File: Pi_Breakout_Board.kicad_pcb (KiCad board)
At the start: 2 copper layers, 56.5 x 65 mm, 70 parts, among them J1 Raspberry_Pi_2_3, J2 Conn_02x04_Odd_Even heater he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, J3 Conn_02x08_Odd_Even thermisto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, J4 Screw_Terminal_01x02, J5 Conn_01x08_Male, J6 Conn_01x08_Male, J7 Conn_01x05_Male uart breakout, Q1 Q_NMOS_GDSD, Q2 Q_NMOS_GDSD, Q3 Q_NMOS_GDSD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

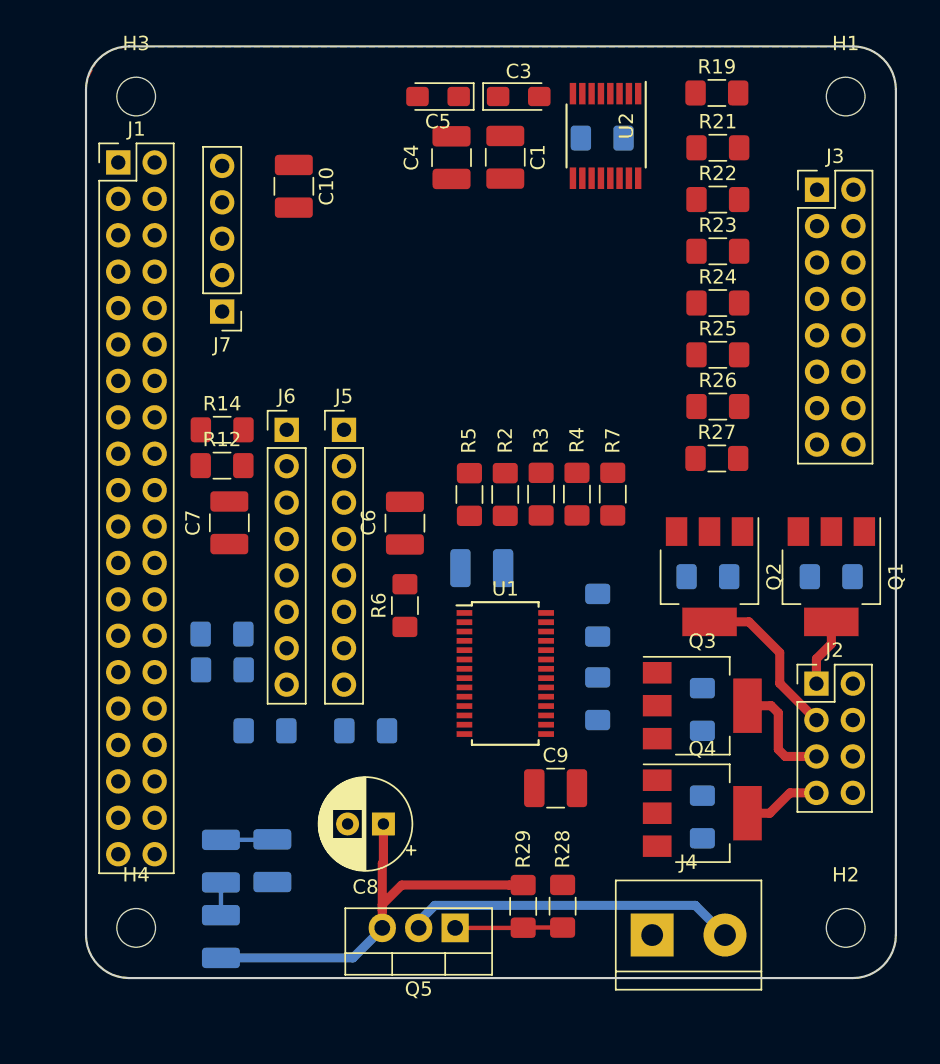
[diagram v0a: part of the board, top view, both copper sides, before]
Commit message: move the PCA9865 from I2C1 to I2C0. Routing saga continues
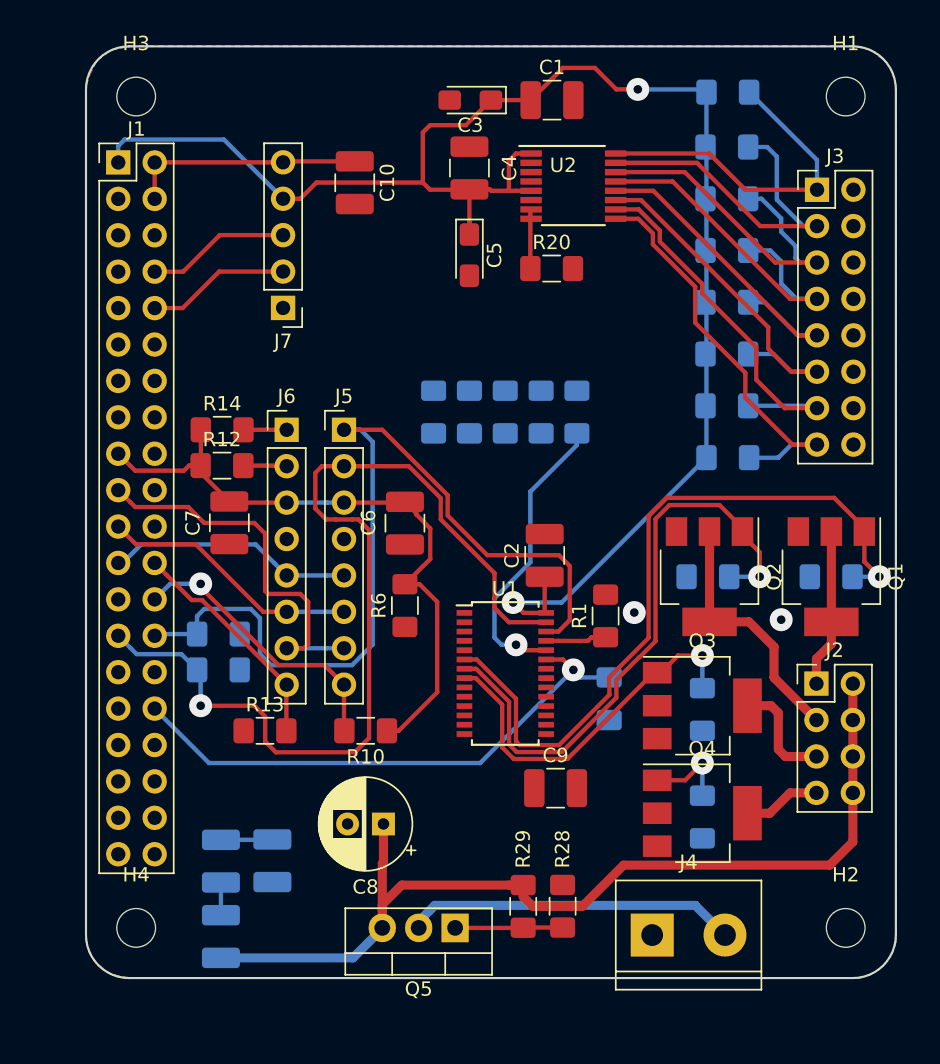
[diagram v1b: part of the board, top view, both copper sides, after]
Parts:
- C2, R1, R10, R13, R20: moved to F.Cu
- R19, R2, R21, R22, R23, R24, R25, R26, R27, R3, R4, R5, R7: moved to B.Cu
- moved C5 11.3 mm to (76.8, 99.6), turned to 270 degrees
- moved R20 9.76 mm to (82.5, 100.5)
- moved R2 7.62 mm to (74.2, 110.5)
- moved R5 7.62 mm to (81.8, 110.5)
- moved R3 7.60 mm to (76.8, 110.5)
- moved R4 7.60 mm to (79.2, 110.5)
- moved R7 6.25 mm to (84.2, 110.5)
- moved C1 5.15 mm to (82.5, 88.8), turned to 0 degrees
- moved C2 4.48 mm to (82.0, 120.5), turned to 90 degrees
- moved C10 4.26 mm to (68.8, 94.5)
- moved J7 4.26 mm to (63.8, 103.2)
- moved U2 4.16 mm to (84.0, 94.8), turned to 0 degrees
- moved C3 3.38 mm to (76.8, 88.8), turned to 180 degrees
- moved C4 1.45 mm to (76.8, 93.5), turned to 90 degrees
- moved R8 0.80 mm to (86.5, 130.5)
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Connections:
- U1 pad 26: SCL1 -> SCL0
- U1 pad 27: SDA1 -> SDA0
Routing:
- net +3V3: track 0.00 -> 159.2 mm, vias 0 -> 2
- net SDA0: track 0.00 -> 68.1 mm, vias 0 -> 1
- net SCL0: track 0.00 -> 63.2 mm
- net Net-(Q1-Pad1): track 0.00 -> 51.5 mm, vias 0 -> 1
- net Net-(Q2-Pad1): track 0.00 -> 43.1 mm, vias 0 -> 1
- net ~OE: track 0.00 -> 38.4 mm, vias 0 -> 1
- net 28V: track 30.3 -> 67.3 mm
- net Net-(J3-Pad15): track 0.00 -> 28.6 mm
- net MOSI0: track 0.00 -> 27.4 mm
- net Net-(J3-Pad13): track 0.00 -> 26.8 mm
- net Net-(Q3-Pad1): track 0.00 -> 25.9 mm, vias 0 -> 1
- net Net-(J3-Pad11): track 0.00 -> 25.2 mm
- net Net-(J3-Pad3): track 0.00 -> 24.7 mm
- net Net-(J3-Pad7): track 0.00 -> 24.6 mm
- net Net-(J3-Pad5): track 0.00 -> 24.4 mm
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- added copper zone on B.Cu, net GND
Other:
- net class Default: via_dia 0.8 -> 1.6; via_drill 0.4 -> 0.6
- net class Power: via_dia 0.8 -> 1.6; via_drill 0.4 -> 0.6

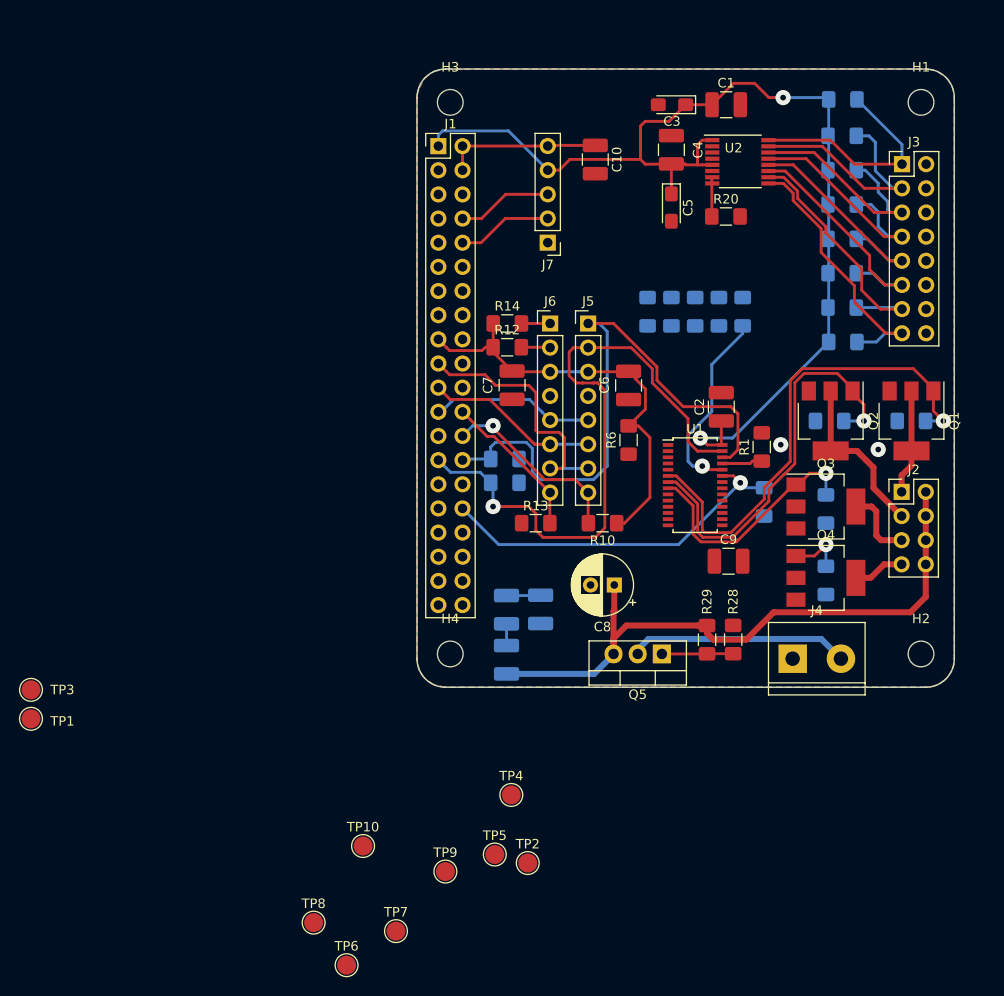
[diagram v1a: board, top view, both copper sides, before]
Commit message: rev3 with corrected header placement in work
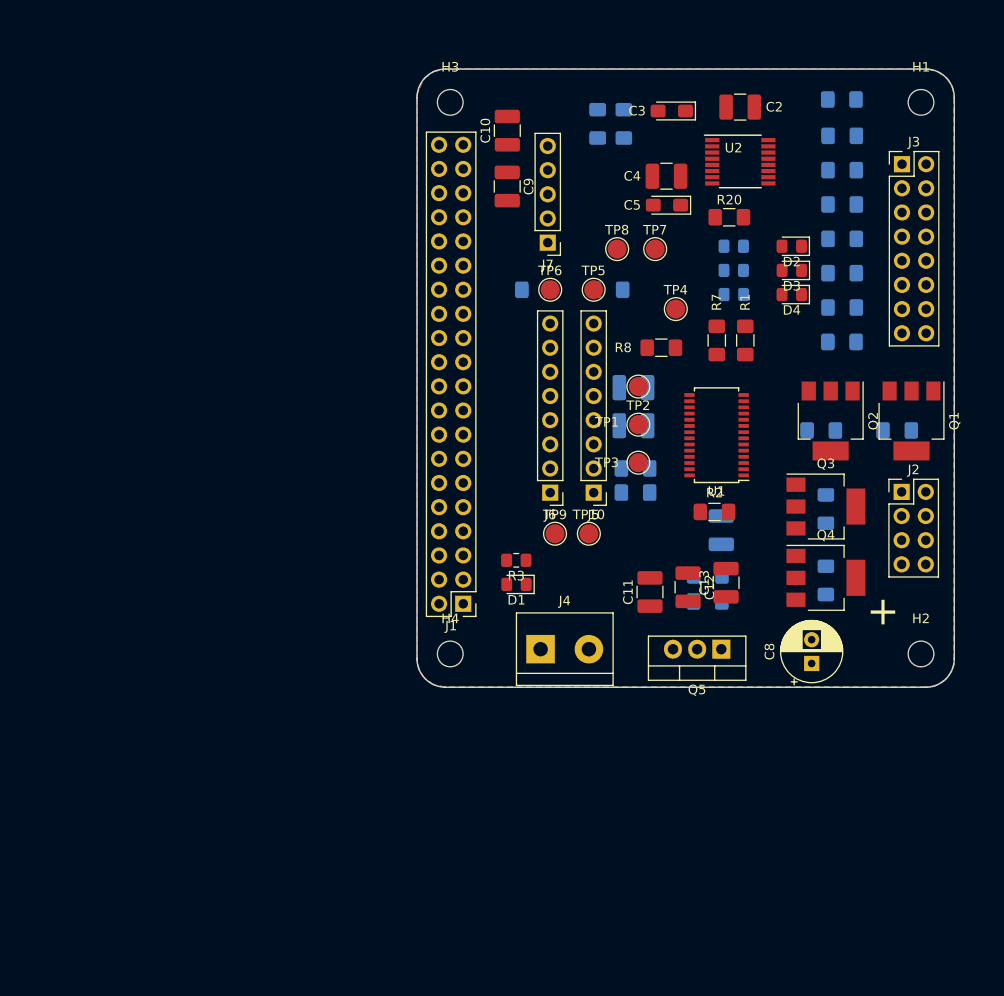
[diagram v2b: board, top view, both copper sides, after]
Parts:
- added D1: LED GREEN, LED_SMD:LED_0805_2012Metric_Pad1.15x1.40mm_HandSolder, F.Cu at (60.5, 139.2)
- added D2: LED GREEN, LED_SMD:LED_0805_2012Metric_Pad1.15x1.40mm_HandSolder, F.Cu at (89.4, 103.6)
- added D3: LED YELLOW, LED_SMD:LED_0805_2012Metric_Pad1.15x1.40mm_HandSolder, F.Cu at (89.4, 106.2)
- added D4: LED RED, LED_SMD:LED_0805_2012Metric_Pad1.15x1.40mm_HandSolder, F.Cu at (89.4, 108.7)
- C1, C6, C7, R10, R12, R13, R14, R28, R29: moved to B.Cu
- C11, C12, C13, R2, R7, R8: moved to F.Cu
- R3: value 10K -> 65R; footprint Resistor_SMD:R_1206_3216Metric_Pad1.42x1.75mm_HandSolder -> Resistor_SMD:R_0805_2012Metric_Pad1.15x1.40mm_HandSolder; moved to F.Cu
- R4, R5: value 10K -> 65R; footprint Resistor_SMD:R_1206_3216Metric_Pad1.42x1.75mm_HandSolder -> Resistor_SMD:R_0805_2012Metric_Pad1.15x1.40mm_HandSolder
- R6: value 10K -> 65R; footprint Resistor_SMD:R_1206_3216Metric_Pad1.42x1.75mm_HandSolder -> Resistor_SMD:R_0805_2012Metric_Pad1.15x1.40mm_HandSolder; moved to B.Cu
- moved TP8 77.7 mm to (71.0, 103.9)
- moved TP7 76.7 mm to (75.0, 103.9)
- moved TP6 74.2 mm to (64.0, 108.2)
- moved TP1 71.0 mm to (73.3, 122.4), turned to 180 degrees
- moved TP3 68.2 mm to (73.3, 126.4), turned to 180 degrees
- moved TP5 60.3 mm to (68.6, 108.2)
- moved TP4 53.9 mm to (77.2, 110.2)
- moved TP2 51.4 mm to (73.3, 118.4), turned to 180 degrees
- moved J1 48.2 mm to (54.9, 141.2), turned to 180 degrees
- moved C9 45.8 mm to (59.5, 97.3), turned to 270 degrees
- moved C1 44.7 mm to (82.0, 133.5), turned to 270 degrees
- moved TP10 40.5 mm to (68.1, 133.9)
- moved TP9 37.3 mm to (64.5, 133.9)
- moved C2 31.6 mm to (84.0, 89.0), turned to 0 degrees
- moved R3 30.8 mm to (60.4, 136.7), turned to 180 degrees
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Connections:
- J1 pad 12: Net-(J1-Pad12) -> LED_GREEN
- J1 pad 16: Net-(J1-Pad16) -> LED_YELLOW
- J1 pad 18: Net-(J1-Pad18) -> LED_RED
- R3 pad 1: Net-(R3-Pad1) -> Net-(D1-Pad1)
- R4 pad 1: Net-(R4-Pad1) -> LED_GREEN
- R4 pad 2: +3V3 -> Net-(D2-Pad2)
- R5 pad 1: Net-(R5-Pad1) -> LED_YELLOW
- R5 pad 2: GND -> Net-(D3-Pad2)
- R6 pad 1: Net-(R6-Pad1) -> LED_RED
- R6 pad 2: +3V3 -> Net-(D4-Pad2)
- U1 pad 2: Net-(R3-Pad1) -> GND
- U1 pad 26: SCL0 -> SCL1
- U1 pad 27: SDA0 -> SDA1
- U1 pad 3: Net-(R4-Pad1) -> +3V3
- U1 pad 4: Net-(R5-Pad1) -> GND
- U1 pad 5: Net-(R6-Pad1) -> +3V3
- U2 pad 2: SDA1 -> SDA0
- U2 pad 3: SCL1 -> SCL0
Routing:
- net +3V3: track 159.2 -> 0.00 mm, vias 2 -> 0
- net SDA0: track 68.1 -> 0.00 mm, vias 1 -> 0
- net 28V: track 67.3 -> 0.00 mm
- net SCL0: track 63.2 -> 0.00 mm
- net Net-(Q1-Pad1): track 51.5 -> 0.00 mm, vias 1 -> 0
- net Net-(Q2-Pad1): track 43.1 -> 0.00 mm, vias 1 -> 0
- net ~OE: track 38.4 -> 0.00 mm, vias 1 -> 0
- net Net-(J3-Pad15): track 28.6 -> 0.00 mm
- net MOSI0: track 27.4 -> 0.00 mm
- net Net-(J3-Pad13): track 26.8 -> 0.00 mm
- net Net-(Q3-Pad1): track 25.9 -> 0.00 mm, vias 1 -> 0
- net Net-(J3-Pad11): track 25.2 -> 0.00 mm
- net Net-(J3-Pad3): track 24.7 -> 0.00 mm
- net Net-(J3-Pad7): track 24.6 -> 0.00 mm
- net Net-(J3-Pad5): track 24.4 -> 0.00 mm
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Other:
- net class Default: trace_width 0.3048 -> 0.4; via_dia 1.6 -> 1.2
- net class Power: trace_width 0.635 -> 1
- rule trace_min: 0.2 -> 0.4
- rule via_min_drill: 0.3 -> 0.6
- rule via_min_size: 0.4 -> 1.2
- board text added: "+"

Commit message: misc routing
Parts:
- removed TP2: TestPoint, TestPoint:TestPoint_Pad_D2.0mm
- added J8: Conn_01x03_Male, Connector_PinHeader_2.54mm:PinHeader_1x03_P2.54mm_Vertical, F.Cu at (63.5, 130.8)
- C10, C9: moved to B.Cu
- J7: value Conn_01x05_Male uart breakout -> Conn_01x02_Female; footprint Connector_PinHeader_2.54mm:PinHeader_1x05_P2.54mm_Vertical -> Connector_PinSocket_2.54mm:PinSocket_1x02_P2.54mm_Horizontal
- R12, R14, R4, R5, R6: moved to F.Cu
- moved R12 50.4 mm to (62.2, 140.2), turned to 180 degrees
- moved C10 49.5 mm to (59.9, 141.0), turned to 0 degrees
- moved R14 45.6 mm to (62.2, 135.9), turned to 180 degrees
- moved J7 42.3 mm to (58.7, 145.3), turned to 90 degrees
- moved R11 39.5 mm to (70.6, 90.1), turned to 270 degrees
- moved C9 38.5 mm to (59.9, 135.9), turned to 0 degrees
- moved TP10 38.2 mm to (59.9, 96.5)
- moved TP9 37.4 mm to (63.5, 96.5)
- moved R9 37.2 mm to (68.1, 90.1), turned to 270 degrees
- moved J6 26.4 mm to (62.7, 103.1), turned to 0 degrees
- moved J5 26.4 mm to (68.1, 103.1), turned to 0 degrees
- moved TP3 20.0 mm to (58.7, 112.8)
- moved C7 18.8 mm to (58.9, 109.7), turned to 270 degrees
- moved TP6 16.3 mm to (62.7, 124.5)
- moved R13 16.3 mm to (61.3, 124.5)
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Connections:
- J1 pad 19: MOSI0 -> Net-(J1-Pad19)
- J7 pad 1: GND -> +5V
- J7 pad 2: RXD -> GND
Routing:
- net +3V3: track 0.00 -> 227.1 mm, vias 0 -> 4
- net SDA1: track 0.00 -> 79.2 mm, vias 0 -> 3
- net SCL1: track 0.00 -> 71.8 mm
- net SDA0: track 0.00 -> 58.7 mm, vias 0 -> 2
- net SCL0: track 0.00 -> 56.7 mm, vias 0 -> 2
- net ~OE: track 0.00 -> 49.3 mm, vias 0 -> 1
- net 28V: track 0.00 -> 47.8 mm
- net Net-(Q1-Pad1): track 0.00 -> 29.3 mm, vias 0 -> 2
- net Net-(J3-Pad15): track 0.00 -> 29.3 mm
- net Net-(Q4-Pad1): track 0.00 -> 27.4 mm, vias 0 -> 2
- net Net-(J3-Pad13): track 0.00 -> 27.3 mm
- net Net-(J3-Pad11): track 0.00 -> 26.0 mm
- net Net-(J3-Pad7): track 0.00 -> 25.2 mm
- net Net-(J3-Pad5): track 0.00 -> 24.8 mm
- net Net-(J3-Pad9): track 0.00 -> 24.8 mm
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
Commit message: routing
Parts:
- C1: moved to F.Cu
- moved R8 6.26 mm to (80.0, 109.8), turned to 90 degrees
- moved TP4 6.25 mm to (80.0, 115.8)
- moved R4 5.68 mm to (87.1, 108.7)
- moved R6 5.68 mm to (87.1, 103.6)
- moved D2 5.68 mm to (91.9, 108.7)
- moved D4 5.68 mm to (91.9, 103.6)
- moved R7 4.61 mm to (86.1, 113.0), turned to 0 degrees
- moved D1 3.62 mm to (67.8, 135.9), turned to 180 degrees
- moved R1 2.95 mm to (86.1, 116.0), turned to 0 degrees
- moved R5 2.54 mm to (87.1, 106.2)
- moved D3 2.54 mm to (92.0, 106.2)
- moved C1 2.05 mm to (81.6, 133.6)
- moved R2 1.55 mm to (81.6, 130.0)
- moved R12 1.52 mm to (62.3, 138.7)
- moved R3 1.48 mm to (67.8, 138.7), turned to 180 degrees
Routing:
- net LED_RED: track 6.11 -> 60.6 mm, vias 0 -> 1
- net LED_GREEN: track 4.78 -> 58.3 mm, vias 0 -> 1
- net LED_YELLOW: track 4.97 -> 58.3 mm, vias 0 -> 1
- net +3V3: track 227.1 -> 211.8 mm, vias 4 -> 3
- net Net-(Q1-Pad1): track 29.3 -> 36.6 mm
- net ~OE: track 49.3 -> 54.4 mm
- net SDA1: track 79.2 -> 74.7 mm
- net ~CE1: track 24.7 -> 28.3 mm
- net ~CE0: track 18.6 -> 22.2 mm
- net Net-(R7-Pad1): track 11.8 -> 15.1 mm
- net Net-(R2-Pad1): track 4.50 -> 2.86 mm
- net Net-(Q2-Pad1): track 20.4 -> 21.9 mm
- net RXD: track 16.6 -> 15.2 mm, vias 0 -> 1
- net Net-(R1-Pad1): track 13.8 -> 12.9 mm
- net GND: vias 0 -> 4

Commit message: Routing updates
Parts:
- R9: moved to F.Cu
- moved R9 19.0 mm to (58.7, 106.6), turned to 90 degrees
- moved R11 13.2 mm to (72.6, 103.1), turned to 180 degrees
- moved TP8 4.49 mm to (68.1, 99.6)
- moved TP10 4.13 mm to (62.7, 99.6)
- moved R12 3.92 mm to (58.7, 140.2), turned to 90 degrees
- moved R3 3.61 mm to (71.4, 139.2), turned to 0 degrees
- moved D1 3.34 mm to (67.3, 139.2)
- moved R14 1.80 mm to (62.0, 137.7), turned to 90 degrees
- moved TP3 1.52 mm to (58.7, 111.3)
- moved C6 1.27 mm to (72.1, 109.7)
- moved C9 1.02 mm to (59.9, 136.9)
- moved TP9 0.92 mm to (62.7, 96.0)
- moved C13 0.84 mm to (85.1, 139.2)
- moved C12 0.84 mm to (81.0, 139.2)
- moved TP7 0.72 mm to (68.1, 96.0)
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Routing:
- net +3V3: track 211.8 -> 229.3 mm
- net SCL0: track 56.7 -> 43.9 mm, vias 2 -> 0
- net SCL1: track 71.6 -> 66.0 mm
- net SDA0: track 58.5 -> 54.6 mm, vias 2 -> 0
- net Net-(Q3-Pad1): track 13.7 -> 17.1 mm
- net +5V: track 13.4 -> 16.0 mm
- net Net-(Q1-Pad1): track 36.6 -> 34.2 mm
- net ~OE: track 54.4 -> 56.8 mm
- net ~CE1: track 28.3 -> 30.6 mm
- net LED_YELLOW: track 58.3 -> 56.3 mm
- net SCLK0: track 13.6 -> 15.2 mm
- net LED_GREEN: track 58.3 -> 56.7 mm
- net LED_RED: track 60.6 -> 59.2 mm
- net Net-(J3-Pad1): track 24.0 -> 25.2 mm
- net 28V: track 47.8 -> 46.7 mm
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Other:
- net class Default: trace_width 0.4 -> 0.3048
- rule trace_min: 0.4 -> 0.3048

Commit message: Renaming + minor revs. Ready for spin 2
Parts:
- C1, C10, C2, C4, C6, C7, C9: value 0.1uF -> 0.1U CERAMIC
- R8: moved to B.Cu
- moved C7 16.8 mm to (75.9, 109.8)
- moved R1 14.1 mm to (74.1, 123.4), turned to 180 degrees
- moved R8 12.7 mm to (76.7, 97.5)
- moved R15 2.97 mm to (102.0, 120.4), turned to 90 degrees
- moved R16 2.74 mm to (93.5, 120.4), turned to 90 degrees
- moved R7 1.80 mm to (84.8, 114.3), turned to 90 degrees
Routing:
- net +3V3: track 229.3 -> 209.7 mm, vias 3 -> 5
- net Net-(Q1-Pad1): track 34.2 -> 25.3 mm
- net Net-(R1-Pad1): track 13.5 -> 4.85 mm
- net Net-(R7-Pad1): track 16.0 -> 13.3 mm
- net ~OE: track 56.8 -> 55.1 mm
- net SDA1: track 75.4 -> 76.7 mm
- net SCL1: track 66.0 -> 67.1 mm
- net 28V: track 46.7 -> 47.6 mm
- net SDA0: track 54.6 -> 55.5 mm
- net Net-(Q4-Pad1): track 28.2 -> 28.8 mm
- net Net-(Q2-Pad1): track 21.8 -> 21.3 mm
- net GND: vias 5 -> 7
